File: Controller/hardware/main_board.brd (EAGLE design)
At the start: 75 x 59 mm, 47 parts, among them IC1 LINEAR_78DT, IC2 40XX_4050D, IC3 LP298XS, IC5 ATMEGA328, U1 CSTNE16M0VH3L000R0, X1 MICROSD_SMD, X4 CON-PHOENIX-508_MST2V

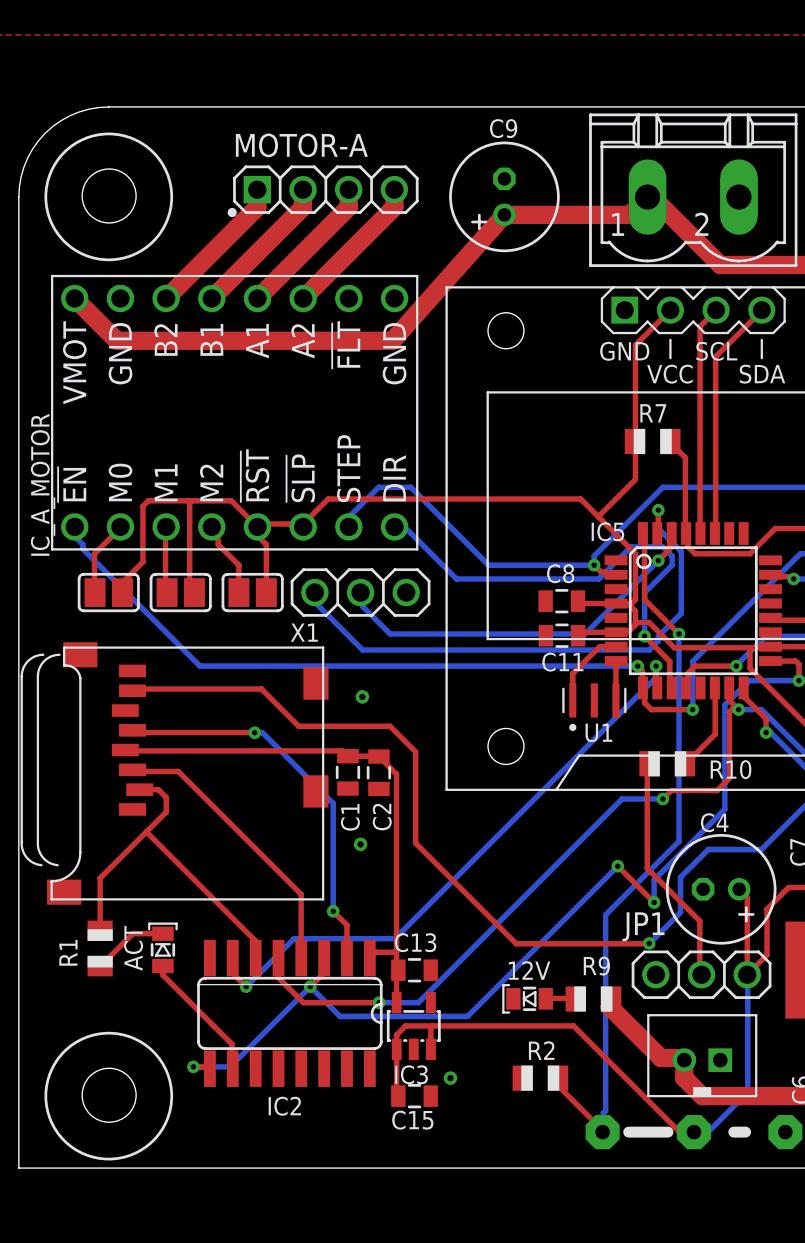
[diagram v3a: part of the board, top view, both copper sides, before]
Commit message: moved 12v indicator next to power source
moved the led next to the screw terminals. I have found people seem to like being able to see if a specific connection is getting power or not rather than having to look around on the board for an indicator and figuring out what it means.
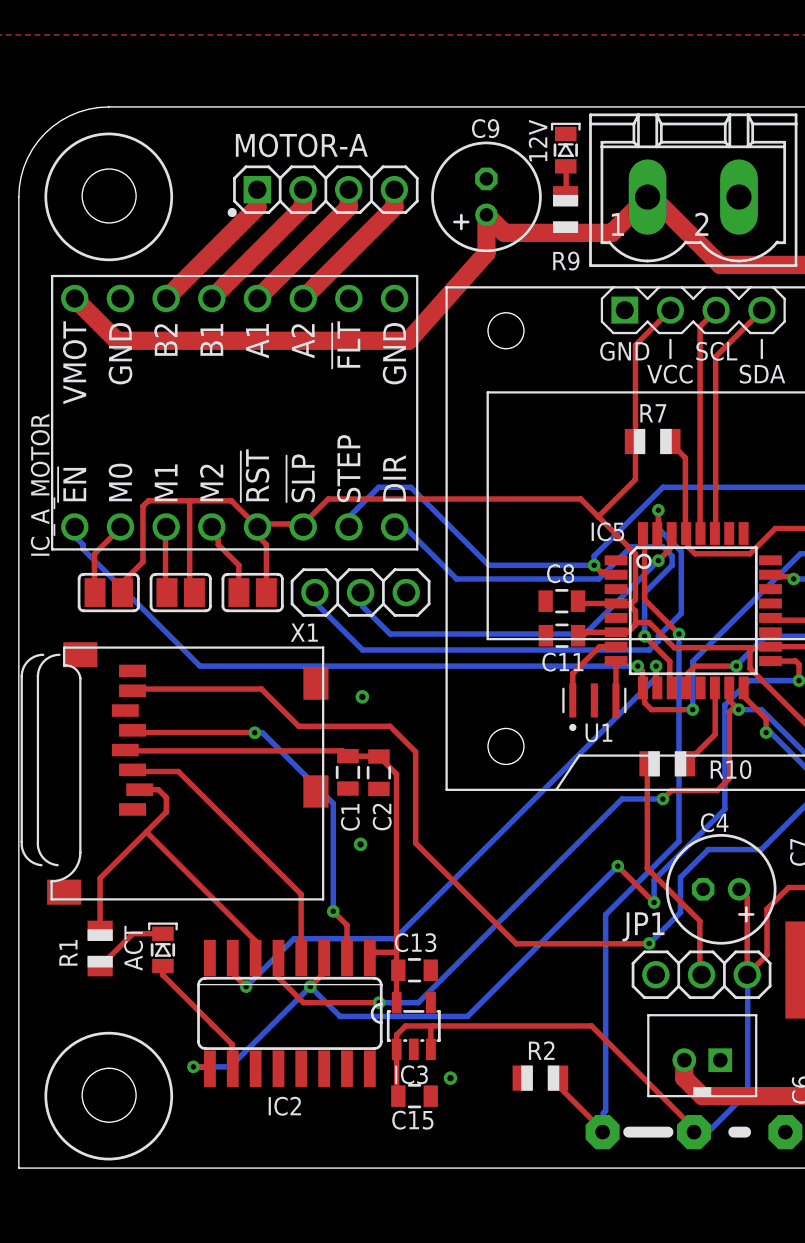
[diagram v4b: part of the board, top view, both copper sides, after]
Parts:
- moved 12V 47.2 mm to (30.4, 56.6), turned to 0 degrees
- moved R9 43.7 mm to (30.4, 53.0), turned to 270 degrees
- moved C9 1.00 mm to (26.0, 54.0)
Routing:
- net +12V: track 137.3 -> 134.0 mm
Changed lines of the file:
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@@
 </autorouter>
 <elements>
-<element name="12V" library="main_board" package="SPARKFUN_LED-0805" value="12v" x="28.4" y="9.41" smashed="yes" rot="R90">
-<attribute name="MFR" value="Würth Elektronik" x="28.4" y="9.41" size="1.778" layer="27" rot="R90" display="off"/>
-<attribute name="MFR_PN" value="150080RS75000" x="28.4" y="9.41" size="1.778" layer="27" rot="R90" display="off"/>
-<attribute name="NAME" x="29.562" y="11.4845" size="1.016" layer="25" rot="R180"/>
-<attribute name="VALUE" x="29.416" y="10.807" size="0.4064" layer="27" rot="R180"/>
-<attribute name="VENDOR" value="digikey" x="28.4" y="9.41" size="1.778" layer="27" rot="R90" display="off"/>
-<attribute name="VENDOR_PN" value="732-4984-1-ND" x="28.4" y="9.41" size="1.778" layer="27" rot="R90" display="off"/>
+<element name="12V" library="main_board" package="SPARKFUN_LED-0805" value="12v" x="30.41" y="56.6" smashed="yes">
+<attribute name="MFR" value="Würth Elektronik" x="30.41" y="56.6" size="1.778" layer="27" display="off"/>
+<attribute name="MFR_PN" value="150080RS75000" x="30.41" y="56.6" size="1.778" layer="27" display="off"/>
+<attribute name="NAME" x="29.3845" y="55.838" size="1.016" layer="25" rot="R90"/>
+<attribute name="VALUE" x="31.807" y="55.584" size="0.4064" layer="27" rot="R90"/>
+<attribute name="VENDOR" value="digikey" x="30.41" y="56.6" size="1.778" layer="27" display="off"/>
+<attribute name="VENDOR_PN" value="732-4984-1-ND" x="30.41" y="56.6" size="1.778" layer="27" display="off"/>
 </element>
 <element name="ACT" library="main_board" package="SPARKFUN_LED-0805" value="ACT" x="8.01" y="12.13" smashed="yes">
@@
 <attribute name="VENDOR_PN" value="RMCF0805FT10K0CT-ND" x="35.24" y="40.4" size="1.778" layer="27" rot="R180" display="off"/>
 </element>
-<element name="R9" library="main_board" package="ADAFRUIT_R0805" value="2.2k" x="31.95" y="9.4" smashed="yes">
-<attribute name="MFR" value="Panasonic Electronic Components" x="31.95" y="9.4" size="1.778" layer="27" display="off"/>
-<attribute name="MFR_PN" value="ERA-6AED222V" x="31.95" y="9.4" size="1.778" layer="27" display="off"/>
-<attribute name="NAME" x="31.288" y="10.7255" size="1.016" layer="25"/>
-<attribute name="VALUE" value="2.2k" x="30.934" y="8.003" size="1.016" layer="27"/>
-<attribute name="VENDOR" value="digikey" x="31.95" y="9.4" size="1.778" layer="27" display="off"/>
-<attribute name="VENDOR_PN" value="P2.2KBNCT-ND" x="31.95" y="9.4" size="1.778" layer="27" display="off"/>
+<element name="R9" library="main_board" package="ADAFRUIT_R0805" value="2.2k" x="30.4" y="53.05" smashed="yes" rot="R270">
+<attribute name="MFR" value="Panasonic Electronic Components" x="30.4" y="53.05" size="1.778" layer="27" rot="R270" display="off"/>
+<attribute name="MFR_PN" value="ERA-6AED222V" x="30.4" y="53.05" size="1.778" layer="27" rot="R270" display="off"/>
+<attribute name="NAME" x="29.588" y="49.9255" size="1.016" layer="25"/>
+<attribute name="VALUE" value="2.2k" x="29.003" y="54.066" size="1.016" layer="27" rot="R270"/>
+<attribute name="VENDOR" value="digikey" x="30.4" y="53.05" size="1.778" layer="27" rot="R270" display="off"/>
+<attribute name="VENDOR_PN" value="P2.2KBNCT-ND" x="30.4" y="53.05" size="1.778" layer="27" rot="R270" display="off"/>
 </element>
 <element name="SW_NEXT" library="main_board" package="ADAFRUIT_EVQ-Q2" value="S_TACT" x="69.69" y="24.42" smashed="yes" rot="R90">
@@
 <attribute name="VENDOR_PN" value="n/a" x="64" y="32" size="1.778" layer="27" rot="R180" display="off"/>
 </element>
-<element name="C9" library="main_board" package="RCL_E3,5-8" value="100uF" x="27" y="54" smashed="yes" rot="R90">
-<attribute name="MFR_PN" value="16ZLH100MEFC5X11" x="27" y="54" size="1.778" layer="27" rot="R90" display="off"/>
-<attribute name="MNF" value="rubycon" x="27" y="54" size="1.778" layer="27" rot="R90" display="off"/>
-<attribute name="NAME" x="27.798" y="58.306" size="1.016" layer="25" ratio="10" rot="R180"/>
-<attribute name="VALUE" value="100uF" x="30.048" y="51.714" size="1.016" layer="27" ratio="10" rot="R90"/>
-<attribute name="VENDOR" value="digikey" x="27" y="54" size="1.778" layer="27" rot="R90" display="off"/>
-<attribute name="VENDOR_PN" value="1189-1148-ND" x="27" y="54" size="1.778" layer="27" rot="R90" display="off"/>
+<element name="C9" library="main_board" package="RCL_E3,5-8" value="100uF" x="26" y="54" smashed="yes" rot="R90">
+<attribute name="MFR_PN" value="16ZLH100MEFC5X11" x="26" y="54" size="1.778" layer="27" rot="R90" display="off"/>
+<attribute name="MNF" value="rubycon" x="26" y="54" size="1.778" layer="27" rot="R90" display="off"/>
+<attribute name="NAME" x="26.798" y="58.306" size="1.016" layer="25" ratio="10" rot="R180"/>
+<attribute name="VALUE" value="100uF" x="29.048" y="51.714" size="1.016" layer="27" ratio="10" rot="R90"/>
+<attribute name="VENDOR" value="digikey" x="26" y="54" size="1.778" layer="27" rot="R90" display="off"/>
+<attribute name="VENDOR_PN" value="1189-1148-ND" x="26" y="54" size="1.778" layer="27" rot="R90" display="off"/>
 </element>
 <element name="C10" library="main_board" package="RCL_E3,5-8" value="100uF" x="48" y="54" smashed="yes" rot="R90">
@@
 <contactref element="C10" pad="+"/>
 <contactref element="JP4" pad="2"/>
-<wire x1="35.7056" y1="6.1176" x2="32.85" y2="8.9732" width="1.016" layer="1"/>
-<wire x1="32.95" y1="9.4" x2="32.85" y2="8.9732" width="1.016" layer="1"/>
-<wire x1="36.9605" y1="6.1176" x2="35.7056" y2="6.1176" width="1.016" layer="1"/>
 <wire x1="36.9605" y1="6.1176" x2="37" y2="6" width="1.016" layer="1"/>
 <wire x1="35.30365" y1="53.91135" x2="38.9997" y2="50.2153" width="1.016" layer="1"/>
@@
 <contactref element="IC_B_MOTOR" pad="16"/>
 <wire x1="3.11" y1="48.35" x2="5.46" y2="46" width="1.016" layer="1"/>
-<wire x1="20.778" y1="46" x2="27" y2="53" width="1.016" layer="1"/>
-<wire x1="5.46" y1="46" x2="20.778" y2="46" width="1.016" layer="1"/>
-<wire x1="34.96" y1="53.99" x2="33.97" y2="53" width="1.016" layer="1"/>
-<wire x1="27" y1="53" x2="33.97" y2="53" width="1.016" layer="1"/>
+<wire x1="26" y1="50.874959375" x2="21.66685625" y2="46" width="1.016" layer="1"/>
+<wire x1="26" y1="50.874959375" x2="26" y2="53" width="1.016" layer="1"/>
+<wire x1="5.46" y1="46" x2="21.66685625" y2="46" width="1.016" layer="1"/>
+<wire x1="34.96" y1="53.99" x2="32.97" y2="52" width="1.016" layer="1"/>
+<wire x1="32.97" y1="52" x2="30" y2="52" width="1.016" layer="1"/>
+<wire x1="30" y1="52" x2="27" y2="52" width="1.016" layer="1"/>
+<wire x1="26" y1="53" x2="27" y2="52" width="1.016" layer="1"/>
 <wire x1="38.9997" y1="50.2153" x2="43.9933" y2="50.2153" width="1.016" layer="1"/>
 <wire x1="46.778" y1="53" x2="48" y2="53" width="1.016" layer="1"/>
@@
 <wire x1="52.2447" y1="46.7553" x2="52.2447" y2="20.7553" width="1.016" layer="1"/>
 <wire x1="56" y1="17" x2="56" y2="11.71" width="1.016" layer="1"/>
+<wire x1="30.4" y1="52.05" x2="30.35" y2="52" width="0.6096" layer="1"/>
+<wire x1="30.35" y1="52" x2="30" y2="52" width="0.6096" layer="1"/>
 </signal>
 <signal name="GND">
@@
 <wire x1="62.1956" y1="21.9956" x2="62.1956" y2="29.8233" width="0.3048" layer="1"/>
 <wire x1="20.941" y1="6.51955" x2="21.01" y2="6.6" width="0.3048" layer="1"/>
-<wire x1="30.8448" y1="7.9" x2="23" y2="7.9" width="0.3048" layer="1"/>
+<wire x1="31.8448" y1="7.9" x2="23" y2="7.9" width="0.3048" layer="1"/>
 <wire x1="23" y1="7.9" x2="21.5" y2="7.9" width="0.3048" layer="1"/>
-<wire x1="36.7056" y1="2.0392" x2="30.8448" y2="7.9" width="0.3048" layer="1"/>
-<wire x1="37.4703" y1="2.0392" x2="36.7056" y2="2.0392" width="0.3048" layer="1"/>
-<wire x1="37.4703" y1="2.0392" x2="37.54" y2="2" width="0.3048" layer="1"/>
+<wire x1="37.54" y1="2" x2="37.54" y2="2.2048" width="0.3048" layer="1"/>
+<wire x1="37.54" y1="2.2048" x2="31.8448" y2="7.9" width="0.3048" layer="1"/>
 <wire x1="40.5291" y1="4.20585" x2="40.5291" y2="10.6711" width="0.3048" layer="16"/>
 <wire x1="40.5291" y1="10.6711" x2="40.5291" y2="10.7058" width="0.3048" layer="16"/>
@@
 <contactref element="12V" pad="A"/>
 <contactref element="R9" pad="1"/>
-<wire x1="29.3135" y1="9.4313" x2="30.97035" y2="9.4313" width="0.3048" layer="1"/>
-<wire x1="30.97035" y1="9.4313" x2="30.95" y2="9.4" width="0.3048" layer="1"/>
-<wire x1="29.3135" y1="9.4313" x2="29.3" y2="9.41" width="0.3048" layer="1"/>
+<wire x1="30.4313" y1="55.6865" x2="30.4313" y2="54.02965" width="0.3048" layer="1"/>
+<wire x1="30.4313" y1="54.02965" x2="30.4" y2="54.05" width="0.3048" layer="1"/>
+<wire x1="30.4313" y1="55.6865" x2="30.41" y2="55.7" width="0.3048" layer="1"/>
 </signal>
 <signal name="A4">

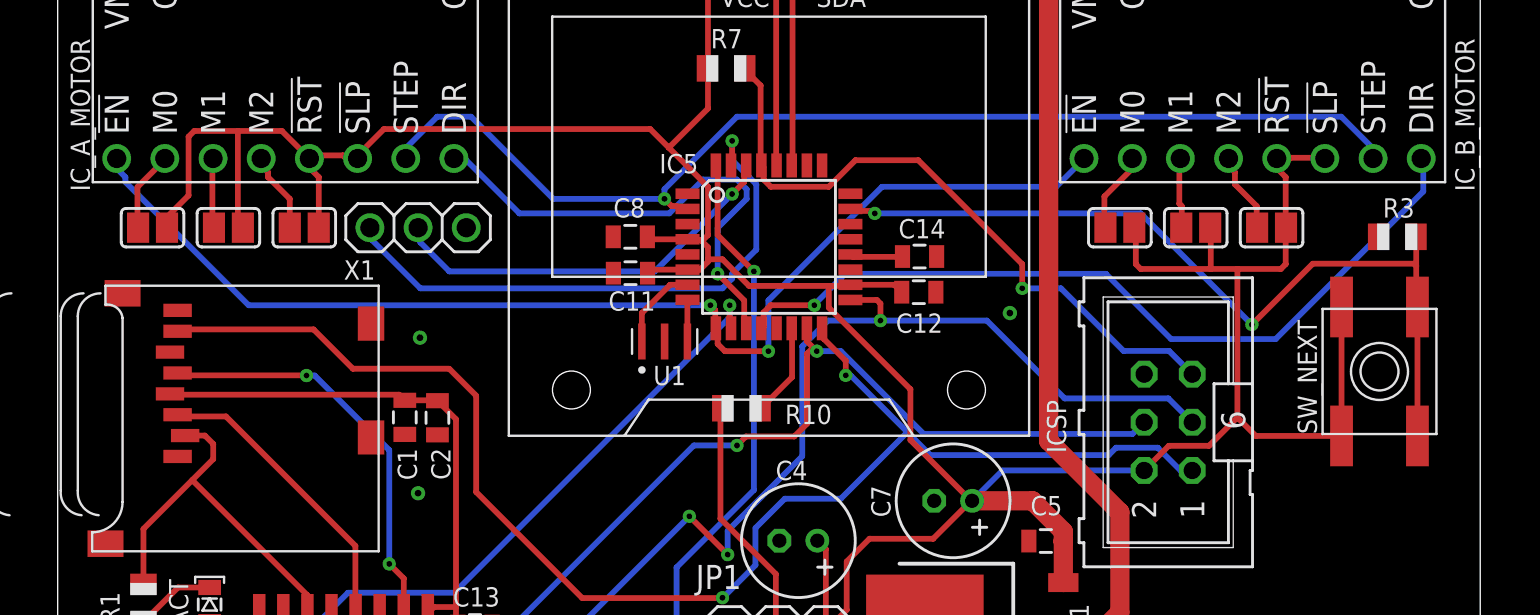
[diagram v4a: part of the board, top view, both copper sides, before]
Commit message: cleaned up traces
finishing up this round of board improvements by cleaning up some traces
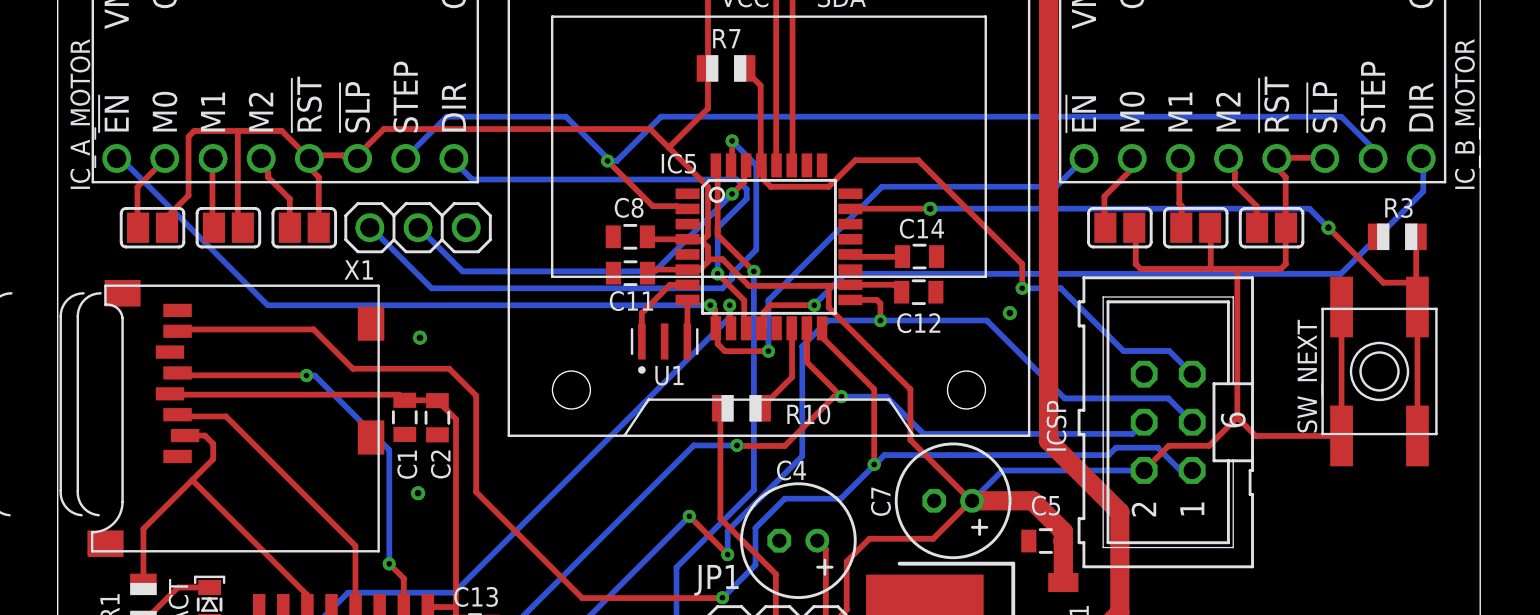
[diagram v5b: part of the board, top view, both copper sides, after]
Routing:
- net D8: track 43.0 -> 40.1 mm
- net A0: track 46.3 -> 43.8 mm
- net D4: track 58.8 -> 60.4 mm
- net D7: track 26.2 -> 24.8 mm
- net D11: track 57.0 -> 55.7 mm
